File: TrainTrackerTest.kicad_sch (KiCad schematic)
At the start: 11 parts, among them J1 PJ-002B, J2 Conn_01x15_Socket, J3 Conn_01x15_Socket, U1 TLC5955DCAR, U2 74HC595D-Q100_118

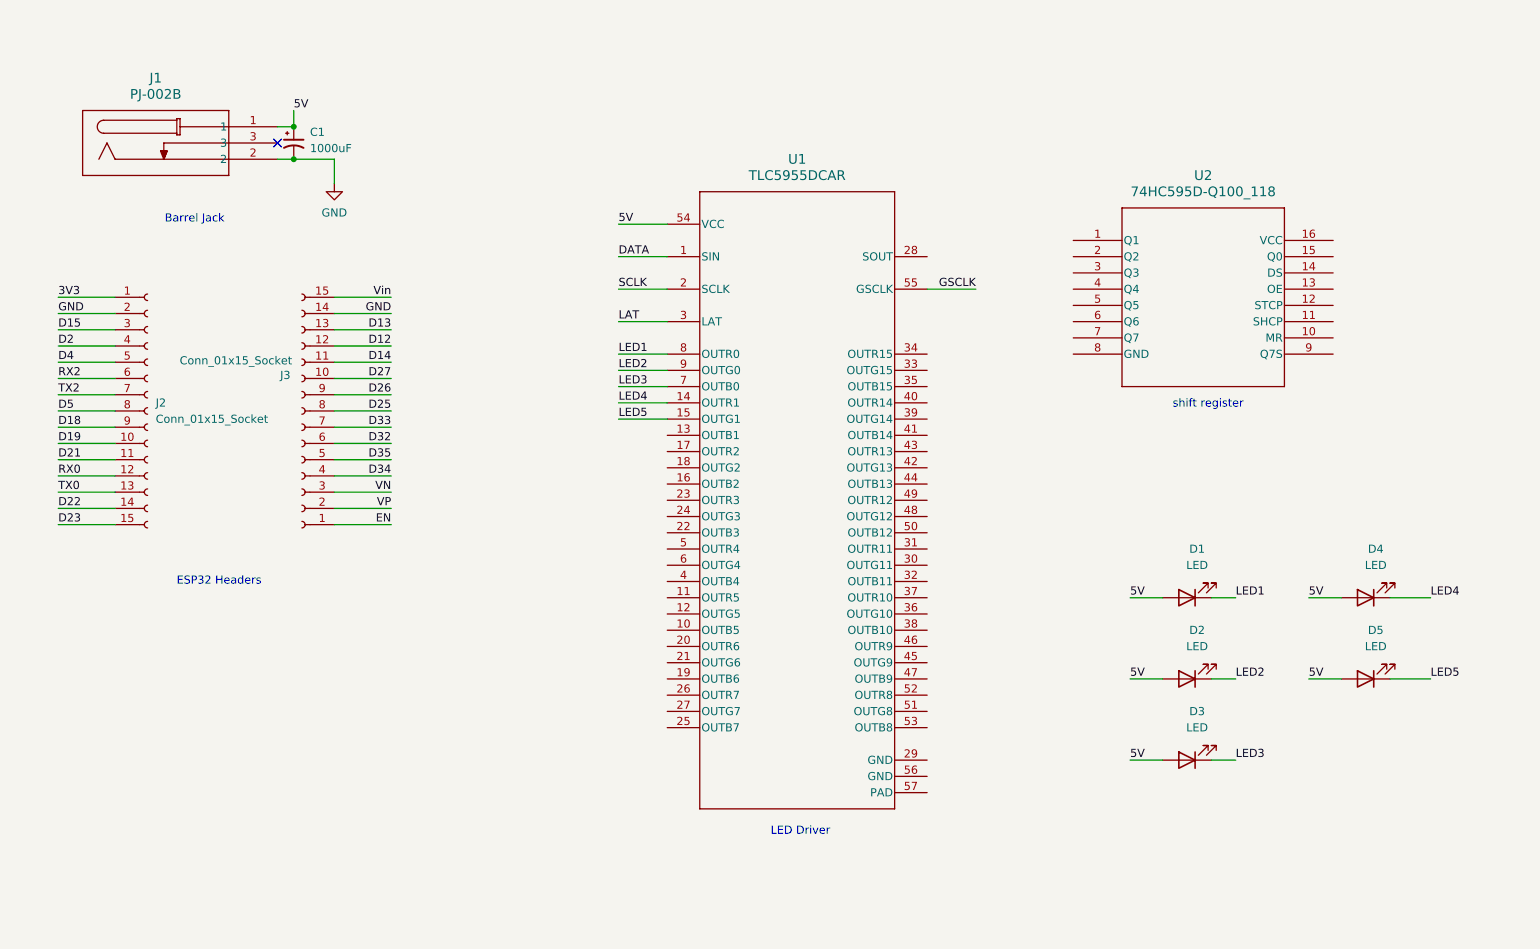
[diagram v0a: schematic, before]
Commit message: Finish first draft of test board
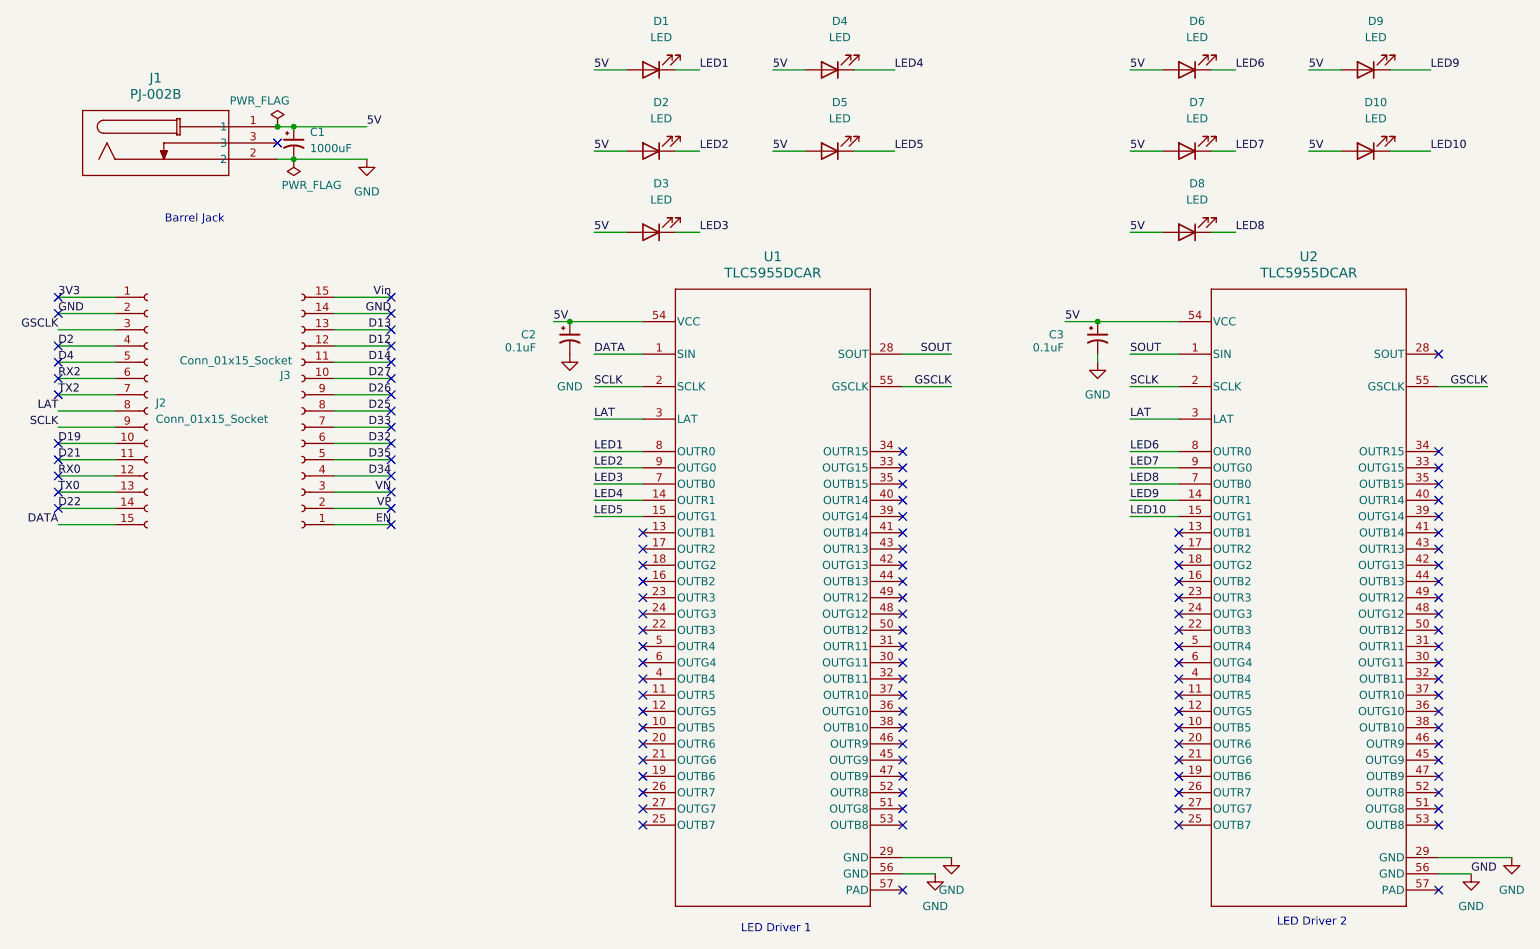
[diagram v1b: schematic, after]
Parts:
- removed U2: 74HC595D-Q100_118, SO16_74HC5_NEX, symbol Shift_Register:74HC595D-Q100_118
- added C2, C3: 0.1uF, Capacitor_SMD:C_0603_1608Metric, symbol Device:C_Polarized_Small_US
- added D10, D6, D7, D8, D9: LED, symbol Device:LED
- added U2: TLC5955DCAR, DCA0056F_N, symbol LED_Driver:TLC5955DCAR
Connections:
- net D15 is gone; now on net GSCLK: J2.3 (Pin_3)
- net D18 is gone; now on net SCLK: J2.9 (Pin_9)
- net D23 is gone; now on net DATA: J2.15 (Pin_15)
- net D5 is gone; now on net LAT: J2.8 (Pin_8)
- net 5V: now also C2.1, C3.1, D10.2 (A), D6.2 (A), D7.2 (A), D8.2 (A), D9.2 (A), U2.54 (VCC)
- net GND: now also U1.29 (GND), U1.56 (GND), C2.2, C3.2, U2.29 (GND), U2.56 (GND)
- net GSCLK: now also U2.55 (GSCLK)
- net LAT: now also U2.3 (LAT)
- net SCLK: now also U2.2 (SCLK)
- net SOUT: now reaches U1.28 (SOUT)
- net SOUT: now also U2.1 (SIN)
- new net LED10: D10.1 (K), U2.15 (OUTG1)
- new net LED6: D6.1 (K), U2.8 (OUTR0)
- new net LED7: D7.1 (K), U2.9 (OUTG0)
- new net LED8: D8.1 (K), U2.7 (OUTB0)
- new net LED9: D9.1 (K), U2.14 (OUTR1)
- no-connect marks 1 -> 116
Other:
- note added: "LED Driver 1"
- note added: "LED Driver 2"
- note removed: "ESP32 Headers"
- note removed: "LED Driver"
- note removed: "shift register"
- moved on the sheet: U1

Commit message: finish layout draft with some DRC failure
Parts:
- D1, D10, D2, D3, D4, D5, D6, D7, D8, D9: footprint (none) -> LED_SMD:LED_0603_1608Metric
- J2, J3: footprint (none) -> Connector_PinHeader_2.54mm:PinHeader_1x15_P2.54mm_Vertical
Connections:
- net GND: now also U1.57 (PAD), U2.57 (PAD)
- no-connect marks 116 -> 114
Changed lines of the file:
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@@
 	)
 	(no_connect
-		(at 252.73 158.75)
-	)
-	(no_connect
 		(at 212.09 135.89)
 	)
@@
 		(at 252.73 138.43)
 	)
-	(no_connect
-		(at 168.91 158.75)
-	)
 	(wire
 		(pts
@@
 			)
 		)
-		(property "Footprint" ""
+		(property "Footprint" "LED_SMD:LED_0603_1608Metric"
 			(at 157.48 43.18 0)
 			(effects
@@
 			)
 		)
-		(property "Footprint" ""
+		(property "Footprint" "LED_SMD:LED_0603_1608Metric"
 			(at 213.36 30.48 0)
 			(effects
@@
 			)
 		)
-		(property "Footprint" ""
+		(property "Footprint" "LED_SMD:LED_0603_1608Metric"
 			(at 129.54 30.48 0)
 			(effects
@@
 	)
 	(symbol
+		(lib_id "power:GND")
+		(at 168.91 158.75 0)
+		(unit 1)
+		(exclude_from_sim no)
+		(in_bom yes)
+		(on_board yes)
+		(dnp no)
+		(fields_autoplaced yes)
+		(property "Reference" "#PWR08"
+			(at 168.91 165.1 0)
+			(effects
+				(font
+					(size 1.27 1.27)
+				)
+				(hide yes)
+			)
+		)
+		(property "Value" "GND"
+			(at 168.91 163.83 0)
+			(effects
+				(font
+					(size 1.27 1.27)
+				)
+			)
+		)
+		(property "Footprint" ""
+			(at 168.91 158.75 0)
+			(effects
+				(font
+					(size 1.27 1.27)
+				)
+				(hide yes)
+			)
+		)
+		(property "Datasheet" ""
+			(at 168.91 158.75 0)
+			(effects
+				(font
+					(size 1.27 1.27)
+				)
+				(hide yes)
+			)
+		)
+		(property "Description" "Power symbol creates a global label with name \"GND\" , ground"
+			(at 168.91 158.75 0)
+			(effects
+				(font
+					(size 1.27 1.27)
+				)
+				(hide yes)
+			)
+		)
+		(pin "1"
+		)
+		(instances
+			(project "TrainTrackerTest"
+				(path "/68b3a549-3f8a-402d-a48f-ea8685749440"
+					(reference "#PWR08")
+					(unit 1)
+				)
+			)
+		)
+	)
+	(symbol
 		(lib_id "Device:LED")
 		(at 129.54 55.88 180)
@@
 			)
 		)
-		(property "Footprint" ""
+		(property "Footprint" "LED_SMD:LED_0603_1608Metric"
 			(at 129.54 55.88 0)
 			(effects
@@
 			)
 		)
-		(property "Footprint" ""
+		(property "Footprint" "LED_SMD:LED_0603_1608Metric"
 			(at 129.54 43.18 0)
 			(effects
@@
 			)
 		)
-		(property "Footprint" ""
+		(property "Footprint" "LED_SMD:LED_0603_1608Metric"
 			(at 213.36 43.18 0)
 			(effects
@@
 			)
 		)
-		(property "Footprint" ""
+		(property "Footprint" "Connector_PinHeader_2.54mm:PinHeader_1x15_P2.54mm_Vertical"
 			(at 74.93 83.82 0)
 			(effects
@@
 			)
 		)
-		(property "Footprint" ""
+		(property "Footprint" "LED_SMD:LED_0603_1608Metric"
 			(at 241.3 43.18 0)
 			(effects
@@
 	)
 	(symbol
+		(lib_id "power:GND")
+		(at 252.73 158.75 0)
+		(unit 1)
+		(exclude_from_sim no)
+		(in_bom yes)
+		(on_board yes)
+		(dnp no)
+		(fields_autoplaced yes)
+		(property "Reference" "#PWR09"
+			(at 252.73 165.1 0)
+			(effects
+				(font
+					(size 1.27 1.27)
+				)
+				(hide yes)
+			)
+		)
+		(property "Value" "GND"
+			(at 252.73 163.83 0)
+			(effects
+				(font
+					(size 1.27 1.27)
+				)
+			)
+		)
+		(property "Footprint" ""
+			(at 252.73 158.75 0)
+			(effects
+				(font
+					(size 1.27 1.27)
+				)
+				(hide yes)
+			)
+		)
+		(property "Datasheet" ""
+			(at 252.73 158.75 0)
+			(effects
+				(font
+					(size 1.27 1.27)
+				)
+				(hide yes)
+			)
+		)
+		(property "Description" "Power symbol creates a global label with name \"GND\" , ground"
+			(at 252.73 158.75 0)
+			(effects
+				(font
+					(size 1.27 1.27)
+				)
+				(hide yes)
+			)
+		)
+		(pin "1"
+		)
+		(instances
+			(project "TrainTrackerTest"
+				(path "/68b3a549-3f8a-402d-a48f-ea8685749440"
+					(reference "#PWR09")
+					(unit 1)
+				)
+			)
+		)
+	)
+	(symbol
 		(lib_id "Device:C_Polarized_Small_US")
 		(at 73.66 41.91 0)
@@
 			)
 		)
-		(property "Footprint" ""
+		(property "Footprint" "LED_SMD:LED_0603_1608Metric"
 			(at 157.48 30.48 0)
 			(effects
@@
 			)
 		)
-		(property "Footprint" ""
+		(property "Footprint" "LED_SMD:LED_0603_1608Metric"
 			(at 213.36 55.88 0)
 			(effects
@@
 			)
 		)
-		(property "Footprint" ""
+		(property "Footprint" "Connector_PinHeader_2.54mm:PinHeader_1x15_P2.54mm_Vertical"
 			(at 50.8 83.82 0)
 			(effects
@@
 			)
 		)
-		(property "Footprint" ""
+		(property "Footprint" "LED_SMD:LED_0603_1608Metric"
 			(at 241.3 30.48 0)
 			(effects

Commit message: Finalize test board pcb layout
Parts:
- removed C1: 1000uF, Capacitor_SMD:C_0603_1608Metric, symbol Device:C_Polarized_Small_US
- removed J1: PJ-002B, PJ-002B_CUI, symbol Barrel_Connector:PJ-002B
- added C5: 1000uF, Capacitor_SMD:C_0603_1608Metric, symbol Device:C_Polarized_Small_US
- added J1: PJ-002B, CUI_PJ-002B, symbol Barrel_Connector_New2:PJ-002B
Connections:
- net 5V: now also C5.1, J1.1
- net GND: now also C5.2, J1.2
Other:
- note removed: "Barrel Jack"

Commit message: Finalized test board pcb layout
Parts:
- renumbered C5 to C1
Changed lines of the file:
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@@
 		(dnp no)
 		(fields_autoplaced yes)
-		(property "Reference" "C5"
+		(property "Reference" "C1"
 			(at 60.96 36.3981 0)
 			(effects
@@
 			(project "TrainTrackerTest"
 				(path "/68b3a549-3f8a-402d-a48f-ea8685749440"
-					(reference "C5")
+					(reference "C1")
 					(unit 1)
 				)

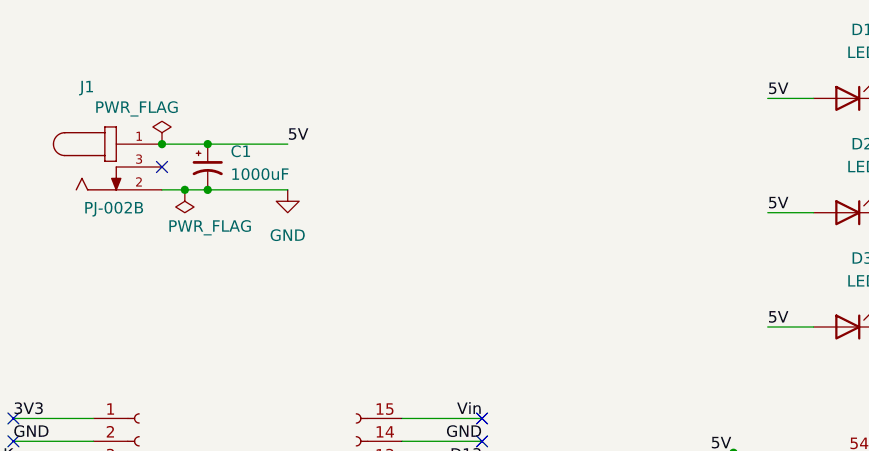
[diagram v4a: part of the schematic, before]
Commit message: Change 1000uF footprint
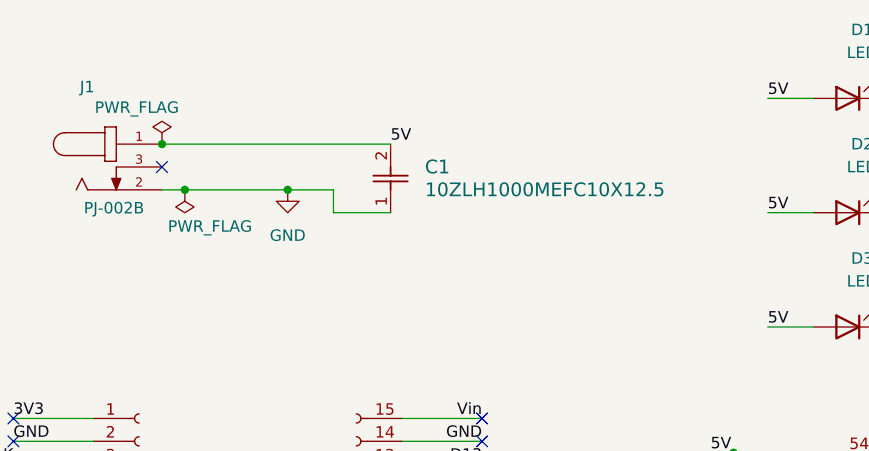
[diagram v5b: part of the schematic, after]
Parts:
- removed C1: 1000uF, Capacitor_SMD:C_0603_1608Metric, symbol Device:C_Polarized_Small_US
- added C1: 10ZLH1000MEFC10X12.5, CAP_10X12.5_RUB, symbol Electrolytic Capacitor:10ZLH1000MEFC10X12.5
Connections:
- net 5V: now also C1.2
- net GND: now also C1.1
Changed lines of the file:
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@@
 	)
 	(junction
-		(at 58.42 40.64)
-		(diameter 0)
-		(color 0 0 0 0)
-	)
-	(junction
-		(at 58.42 35.56)
+		(at 67.31 40.64)
 		(diameter 0)
 		(color 0 0 0 0)
@@
 	(wire
 		(pts
-			(xy 58.42 35.56) (xy 67.31 35.56)
-		)
-		(stroke
-			(width 0)
-			(type default)
-		)
-	)
-	(wire
-		(pts
 			(xy 88.9 83.82) (xy 80.01 83.82)
 		)
@@
 	(wire
 		(pts
-			(xy 53.34 35.56) (xy 58.42 35.56)
+			(xy 53.34 35.56) (xy 78.74 35.56)
 		)
 		(stroke
@@
 	(wire
 		(pts
+			(xy 78.74 43.18) (xy 72.39 43.18)
+		)
+		(stroke
+			(width 0)
+			(type default)
+		)
+	)
+	(wire
+		(pts
 			(xy 204.47 74.93) (xy 212.09 74.93)
 		)
@@
 	(wire
 		(pts
+			(xy 72.39 40.64) (xy 67.31 40.64)
+		)
+		(stroke
+			(width 0)
+			(type default)
+		)
+	)
+	(wire
+		(pts
 			(xy 168.91 156.21) (xy 173.99 156.21)
 		)
@@
 	(wire
 		(pts
-			(xy 58.42 40.64) (xy 55.88 40.64)
+			(xy 55.88 40.64) (xy 67.31 40.64)
 		)
 		(stroke
@@
 	(wire
 		(pts
-			(xy 36.83 91.44) (xy 45.72 91.44)
+			(xy 72.39 43.18) (xy 72.39 40.64)
 		)
 		(stroke
@@
 	(wire
 		(pts
-			(xy 167.64 30.48) (xy 161.29 30.48)
+			(xy 36.83 91.44) (xy 45.72 91.44)
 		)
 		(stroke
@@
 	(wire
 		(pts
-			(xy 67.31 40.64) (xy 58.42 40.64)
+			(xy 167.64 30.48) (xy 161.29 30.48)
 		)
 		(stroke
@@
 	)
 	(label "5V"
-		(at 67.31 35.56 0)
+		(at 78.74 35.56 0)
 		(fields_autoplaced yes)
 		(effects
@@
 	)
 	(symbol
-		(lib_id "Device:C_Polarized_Small_US")
-		(at 58.42 38.1 0)
-		(unit 1)
-		(exclude_from_sim no)
-		(in_bom yes)
-		(on_board yes)
-		(dnp no)
-		(fields_autoplaced yes)
-		(property "Reference" "C1"
-			(at 60.96 36.3981 0)
-			(effects
-				(font
-					(size 1.27 1.27)
-				)
-				(justify left)
-			)
-		)
-		(property "Value" "1000uF"
-			(at 60.96 38.9381 0)
-			(effects
-				(font
-					(size 1.27 1.27)
-				)
-				(justify left)
-			)
-		)
-		(property "Footprint" "Capacitor_SMD:C_0603_1608Metric"
-			(at 58.42 38.1 0)
-			(effects
-				(font
-					(size 1.27 1.27)
-				)
-				(hide yes)
-			)
-		)
-		(property "Datasheet" "~"
-			(at 58.42 38.1 0)
-			(effects
-				(font
-					(size 1.27 1.27)
-				)
-				(hide yes)
-			)
-		)
-		(property "Description" ""
-			(at 58.42 38.1 0)
-			(effects
-				(font
-					(size 1.27 1.27)
-				)
-				(hide yes)
-			)
-		)
-		(pin "1"
-		)
-		(pin "2"
-		)
-		(instances
-			(project "TrainTrackerTest"
-				(path "/68b3a549-3f8a-402d-a48f-ea8685749440"
-					(reference "C1")
-					(unit 1)
-				)
-			)
-		)
-	)
-	(symbol
 		(lib_id "LED_Driver:TLC5955DCAR")
 		(at 232.41 113.03 0)
@@
 					(unit 1)
 				)
+			)
+		)
+	)
+	(symbol
+		(lib_id "Electrolytic Capacitor:10ZLH1000MEFC10X12.5")
+		(at 78.74 43.18 90)
+		(unit 1)
+		(exclude_from_sim no)
+		(in_bom yes)
+		(on_board yes)
+		(dnp no)
+		(fields_autoplaced yes)
+		(property "Reference" "C1"
+			(at 82.55 38.0999 90)
+			(effects
+				(font
+					(size 1.524 1.524)
+				)
+				(justify right)
+			)
+		)
+		(property "Value" "10ZLH1000MEFC10X12.5"
+			(at 82.55 40.6399 90)
+			(effects
+				(font
+					(size 1.524 1.524)
+				)
+				(justify right)
+			)
+		)
+		(property "Footprint" "CAP_10X12.5_RUB"
+			(at 78.74 43.18 0)
+			(effects
+				(font
+					(size 1.27 1.27)
+					(italic yes)
+				)
+				(hide yes)
+			)
+		)
+		(property "Datasheet" "10ZLH1000MEFC10X12.5"
+			(at 78.74 43.18 0)
+			(effects
+				(font
+					(size 1.27 1.27)
+					(italic yes)
+				)
+				(hide yes)
+			)
+		)
+		(property "Description" ""
+			(at 78.74 43.18 0)
+			(effects
+				(font
+					(size 1.27 1.27)
+				)
+				(hide yes)
+			)
+		)
+		(pin "1"
+		)
+		(pin "2"
+		)
+		(instances
+			(project ""
+				(path "/68b3a549-3f8a-402d-a48f-ea8685749440"
+					(reference "C1")
+					(unit 1)
+				)
